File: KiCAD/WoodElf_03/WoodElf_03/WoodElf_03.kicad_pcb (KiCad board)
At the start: 2 copper layers, 13 parts, among them T1 BlankThrough-Hole, T10 BlankThrough-Hole, T2 BlankThrough-Hole, T3 BlankThrough-Hole, T4 BlankThrough-Hole, T5 BlankThrough-Hole, T6 BlankThrough-Hole, T9 BlankThrough-Hole

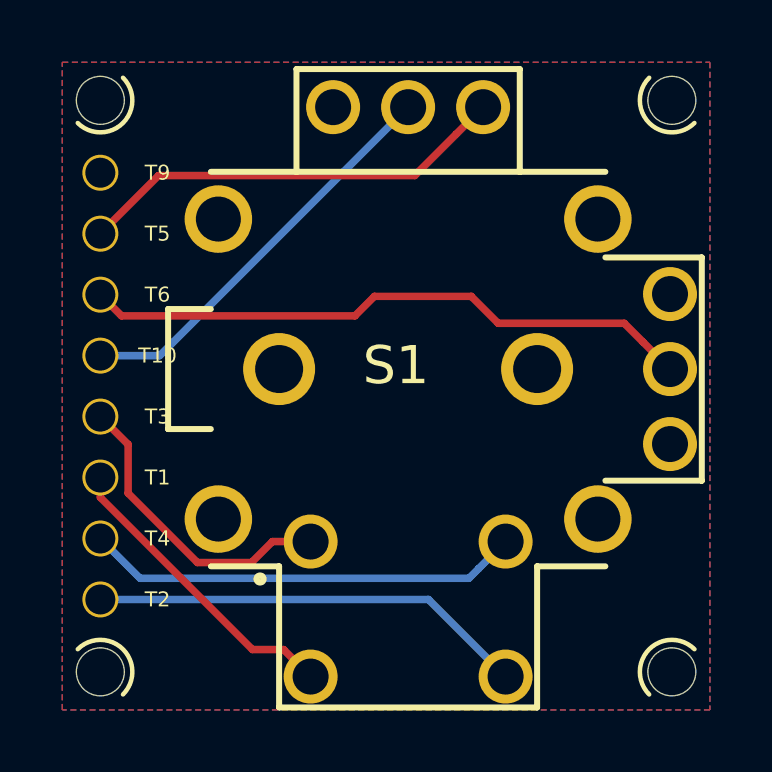
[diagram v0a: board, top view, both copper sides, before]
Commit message: reworked the outer edge of the PCB
turns out i didnt consider how the tiling screw holes would fit with the wire holes - it should all be good now and not interfere with itself
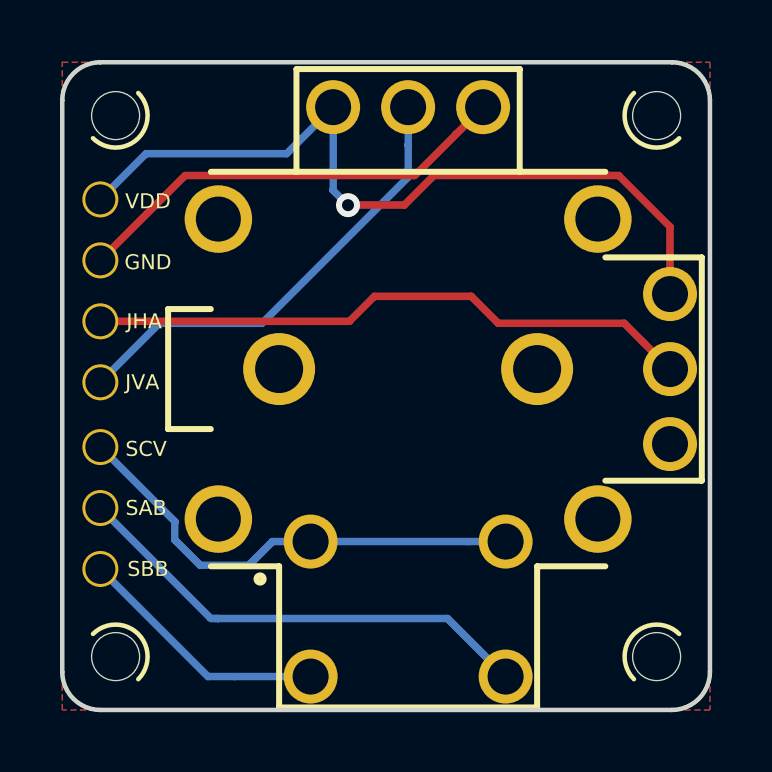
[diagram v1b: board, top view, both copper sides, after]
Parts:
- removed T4: BlankThrough-Hole, WoodElf_Lib:BlankThrough-Hole
- moved T1 3.05 mm to (57.4, 46.6)
- moved T2 3.05 mm to (57.4, 44.6)
- moved T3 1.02 mm to (57.4, 42.5)
- moved T10 0.89 mm to (57.4, 40.4)
- moved T5 0.89 mm to (57.4, 36.3)
- moved T6 0.89 mm to (57.4, 38.4)
- moved T9 0.89 mm to (57.4, 34.3)
- moved Mount 0.72 mm to (75.9, 31.5)
- moved Mount 0.72 mm to (57.9, 31.5)
- moved Mount 0.72 mm to (57.9, 49.5)
- moved Mount 0.72 mm to (75.9, 49.5)
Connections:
- S1 pad 3: /C -> /A
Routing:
- net /3_1: track 0.00 -> 26.6 mm, vias 0 -> 1
- net /C: track 14.6 -> 0.00 mm
- net /A: track 10.3 -> 15.8 mm
- net /2_2: track 13.7 -> 15.4 mm
- net /B: track 10.1 -> 8.49 mm
- net /D: track 14.6 -> 16.0 mm
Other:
- board outline added: 21.6 x 21.6 mm
- board text added: "GND"
- board text added: "JHA"
- board text added: "JVA"
- board text added: "SAB"
- board text added: "SBB"
- board text added: "SCV"
- board text added: "VDD"
